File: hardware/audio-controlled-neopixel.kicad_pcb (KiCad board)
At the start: 2 copper layers, 96 x 56 mm, 62 parts, among them J1 AudioJack4, J10 Conn_01x04_Male, J2 AudioJack4, J3 KF2EDGK, J4 KF2EDGK, J5 KF2EDGK, J6 Conn_01x01_Female, J7 Conn_01x01_Female, J8 Conn_01x01_Female, J9 Conn_01x01_Female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

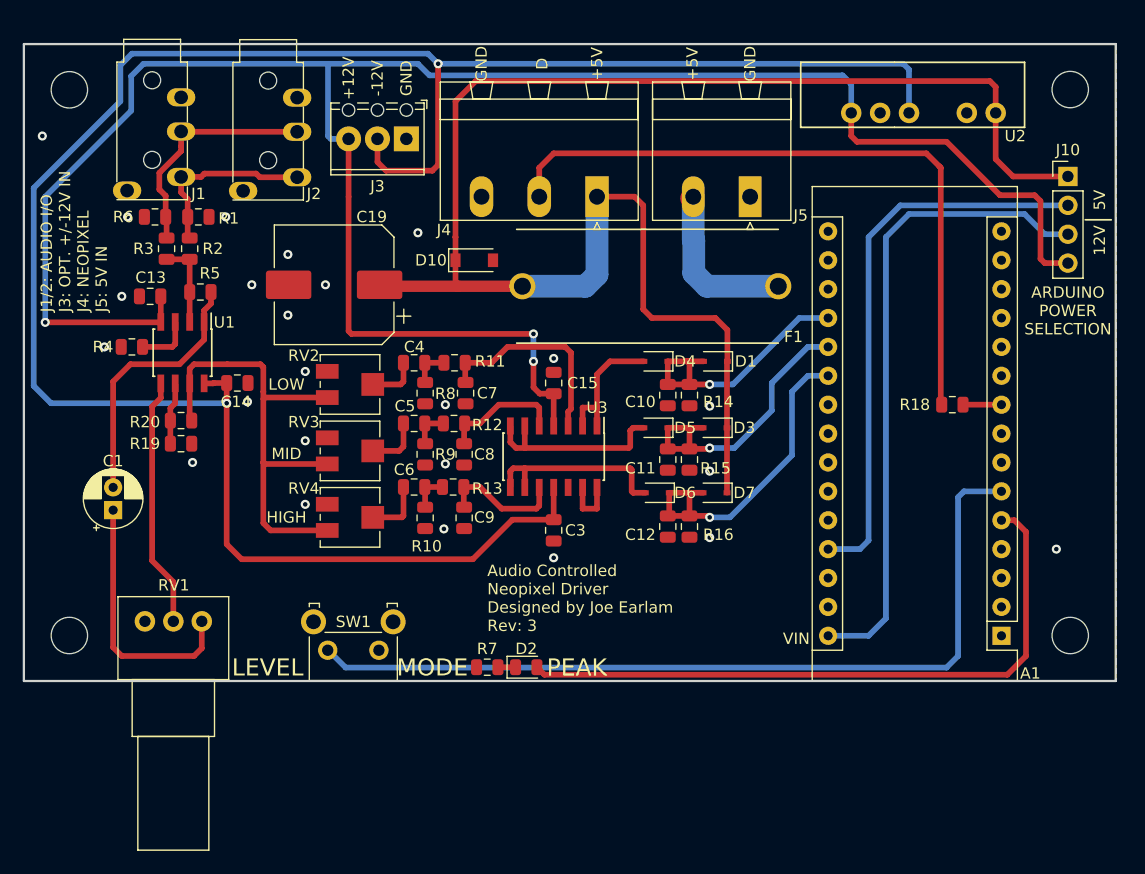
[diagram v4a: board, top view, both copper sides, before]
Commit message: added power supply filtering
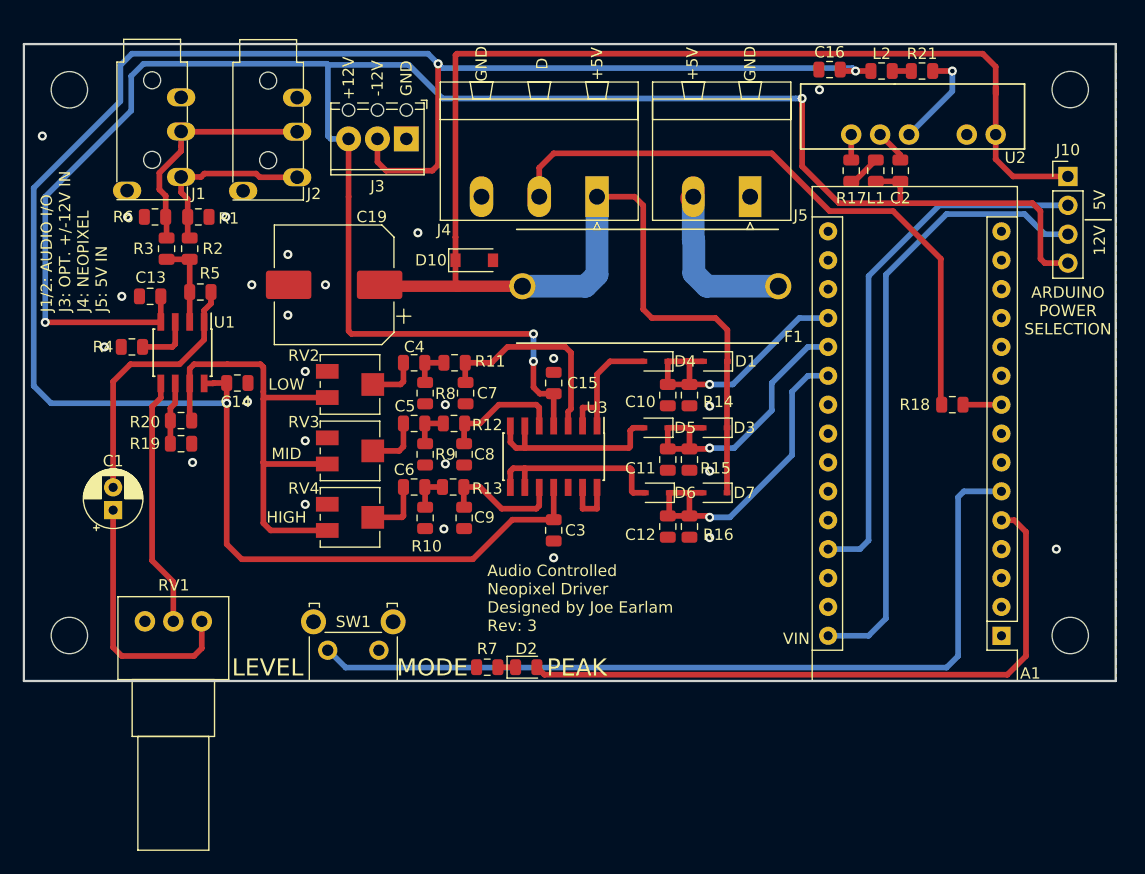
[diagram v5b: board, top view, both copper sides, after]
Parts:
- added C16: 10u, Capacitor_SMD:C_0805_2012Metric, F.Cu at (108.8, 31.2)
- added C2: 10u, Capacitor_SMD:C_0805_2012Metric, F.Cu at (115.1, 40.1)
- added L1: 10u, Inductor_SMD:L_0805_2012Metric, F.Cu at (112.9, 40.1)
- added L2: 10u, Inductor_SMD:L_0805_2012Metric, F.Cu at (113.4, 31.4)
- added R17: 1R, Resistor_SMD:R_0805_2012Metric, F.Cu at (110.7, 40.1)
- added R21: 1R, Resistor_SMD:R_0805_2012Metric, F.Cu at (117.0, 31.4)
- moved U2 1.91 mm to (126.0, 32.5)
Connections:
- U2 pad 4: -12V -> Net-(R21-Pad2)
- U2 pad 6: +12V -> Net-(R17-Pad2)
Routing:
- net Net-(R21-Pad2): track 0.00 -> 8.90 mm, vias 0 -> 1
- net +5V: track 140.6 -> 146.6 mm
- net -12V: track 189.6 -> 184.3 mm, vias 2 -> 3
- net /Neopixel: track 59.9 -> 55.2 mm
- net +12V: track 184.0 -> 188.3 mm, vias 3 -> 4
- net GND: track 0.00 -> 2.97 mm, vias 24 -> 25
- net Net-(L1-Pad1): track 0.00 -> 2.94 mm
- net Net-(R17-Pad2): track 0.00 -> 2.24 mm
- net Net-(A1-Pad27): track 49.2 -> 47.2 mm
- net Net-(A1-Pad30): track 56.8 -> 54.9 mm
- net Net-(L2-Pad1): track 0.00 -> 1.68 mm
